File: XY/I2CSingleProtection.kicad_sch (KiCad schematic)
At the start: 9 parts, among them Q7 NX3008NBKS, Q8 MBT2222ADW1T1

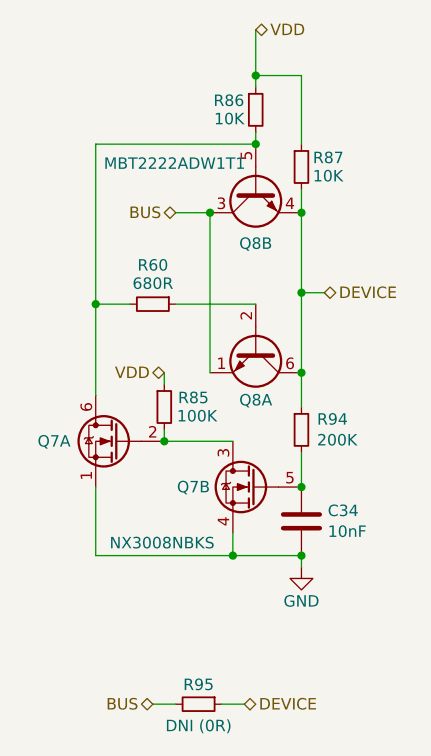
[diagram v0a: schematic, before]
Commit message: Updated layout
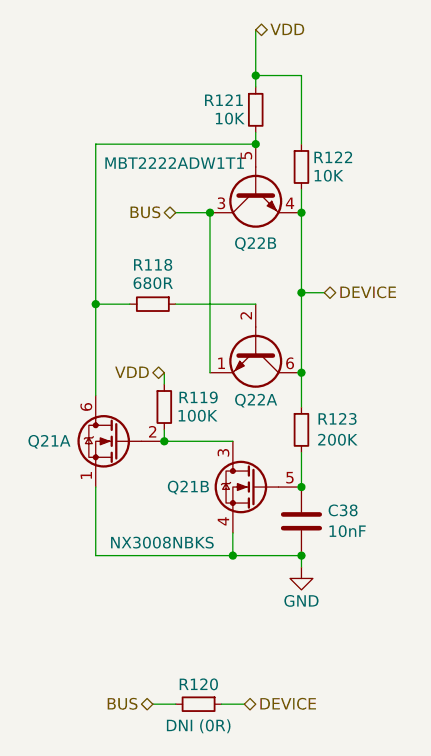
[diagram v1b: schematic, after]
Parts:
- renumbered C34 to C38, Q7 to Q21, Q8 to Q22, R60 to R118, R85 to R119, R95 to R120, R86 to R121, R87 to R122, R94 to R123
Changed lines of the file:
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@@
 		(on_board yes)
 		(dnp no)
-		(property "Reference" "R94"
+		(property "Reference" "R123"
 			(at 150.3172 95.3516 0)
 			(effects
@@
 		(on_board yes)
 		(dnp no)
-		(property "Reference" "R85"
+		(property "Reference" "R119"
 			(at 134.874 92.964 0)
 			(effects
@@
 		(on_board yes)
 		(dnp no)
-		(property "Reference" "C34"
+		(property "Reference" "C38"
 			(at 151.511 105.5116 0)
 			(effects
@@
 		(on_board yes)
 		(dnp no)
-		(property "Reference" "R60"
+		(property "Reference" "R118"
 			(at 132.08 78.232 90)
 			(effects
@@
 		(on_board yes)
 		(dnp no)
-		(property "Reference" "Q7"
+		(property "Reference" "Q21"
 			(at 122.936 97.79 0)
 			(effects
@@
 		(on_board yes)
 		(dnp no)
-		(property "Reference" "Q8"
+		(property "Reference" "Q22"
 			(at 143.51 93.218 90)
 			(effects
@@
 		(on_board yes)
 		(dnp no)
-		(property "Reference" "Q8"
+		(property "Reference" "Q22"
 			(at 143.51 75.819 90)
 			(effects
@@
 		(on_board yes)
 		(dnp no)
-		(property "Reference" "#PWR045"
+		(property "Reference" "#PWR055"
 			(at 148.59 118.11 0)
 			(effects
@@
 		(on_board yes)
 		(dnp no)
-		(property "Reference" "Q7"
+		(property "Reference" "Q21"
 			(at 138.43 102.87 0)
 			(effects
@@
 		(on_board yes)
 		(dnp no)
-		(property "Reference" "R87"
+		(property "Reference" "R122"
 			(at 149.86 66.294 0)
 			(effects
@@
 		(on_board yes)
 		(dnp no)
-		(property "Reference" "R86"
+		(property "Reference" "R121"
 			(at 142.24 59.944 0)
 			(effects
@@
 		(on_board yes)
 		(dnp no)
-		(property "Reference" "R95"
+		(property "Reference" "R120"
 			(at 137.16 124.841 90)
 			(effects

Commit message: almost done
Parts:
- Q21: symbol mainboard:NX3008NBKS -> Argus-Miscellaneous:NX3008NBKS
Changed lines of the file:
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@@
 	)
 	(symbol
-		(lib_id "mainboard:NX3008NBKS")
+		(lib_id "Argus-Miscellaneous:NX3008NBKS")
 		(at 127 97.79 0)
 		(mirror y)
@@
 	)
 	(symbol
-		(lib_id "mainboard:NX3008NBKS")
+		(lib_id "Argus-Miscellaneous:NX3008NBKS")
 		(at 142.24 102.87 0)
 		(mirror y)
